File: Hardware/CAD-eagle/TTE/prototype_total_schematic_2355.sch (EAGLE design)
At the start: 46 parts, among them IC5 FT230XS, U1 LTC1069-7CS8#PBF, U3 LTC1563-2CGNSSOP-16_GN-M, U7 NX3L2467PW

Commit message: Nightly build. Hopefully final version.
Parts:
- removed C11: 100nF, SparkFun-Capacitors:22UF-0805-6.3V-20%
- removed C4, C8: 22uF, SparkFun-Capacitors:22UF-0805-6.3V-20%
- removed C9: 10nF, SparkFun-Capacitors:22UF-0805-6.3V-20%
- removed CR1: USBLC6-2SC6, TTE:USBLC6-2SC6
- removed D1, D2: (no value), diode:ZENER-DIODESMB
- removed IC5: FT230XS, ftdi:FT230XS
- removed L1: (no value), dp_devices:FERRITE-0805
- removed LED1, LED2: (no value), microbuilder:LED0805
- removed LED4: RGB, microbuilder:LED0805
- removed R10, R11: 27, microbuilder:RESISTOR0805_NOTHERMALS
- removed R12, R13, R14, R15: 10k, SparkFun-Resistors:2.0KOHM-0603-1/10W-5%
- removed R16, R7, R8, R9: 442, SparkFun-Resistors:2.0KOHM-0603-1/10W-5%
- removed R2, R6: 330, SparkFun-Resistors:2.0KOHM-0603-1/10W-5%
- removed TERMINAL_BLOCK1: ED555/2DS, DC_LOAD_AU:ED555/2DS
- removed X2: (no value), BeagleBone_Black_Wireless:GHI-CONNECTORS_10118192-0001LF
- added C17: 1.1nF, SparkFun-Capacitors:22UF-0805-6.3V-20%
- added C18: 10µF, SparkFun-Capacitors:10UF-POLAR-EIA6032-25V-10%
- added CN1: HOST, adafruit:USBMINIB
- added JP2: (no value), adafruit:PINHD-1X8-3.5MM
- added LED3, RXLED, TXLED: (no value), led:LEDCHIP-LED0603
- added R17: 1k, SparkFun-Resistors:2.0KOHM-0603-1/10W-5%
- added R18: 33k, SparkFun-Resistors:2.0KOHM-0603-1/10W-5%
- added R19: 330, SparkFun-Resistors:2.0KOHM-0603-1/10W-5%
- added R20, R25: 330, rcl:R-US_R0603
- added RIGHT_ANGLE_SMA_MALE: 5-1814400-1, TTE:5-1814400-1
- added S2: MOMENTARY-SWITCH-SPST-PTH-6.0MM, SparkFun-Switches:MOMENTARY-SWITCH-SPST-PTH-6.0MM
- added TM1: (no value), adafruit:TRIMPOTTC33X
- added U$1: AZ23C3V3, TTE:AZ23C3V3
- added U2: FT232RL-BASICSSOP, SparkFun:FT232RL-BASICSSOP
- C15: value 110n -> 470n
- C16: value 110n -> 100n
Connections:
- removed net !RESET: IC5.!RESET
- removed net 0: C11.2, C4.2, C8.2, C9.2
- removed net CTS_BAR: IC5.!CTS, R12.2
- removed net D+: C8.1, CR1.I/O2_2, R11.1, X2.SGND3
- removed net D-: C4.1, CR1.I/O1_2, R10.1, X2.SGND4
- removed net ID: X2.SGND2
- removed net N$3: LED1.A, LED2.A, R6.1
- removed net N$4: LED4.A, R2.1
- removed net N$50: U$5.P2.5/COMP1.0
- removed net PWR_EN_BAR: IC5.CBUS0
- removed net RESET_BAR: C11.1, IC5.VCCIO, R12.1, R13.1, R14.1, R15.1
- removed net RTS_BAR: IC5.!RTS, R13.2, U$5.TEST/SBWTCK
- removed net RX_LED: IC5.CBUS1, LED1.C
- removed net STATUS: IC5.CBUS2, LED2.C, LED4.C
- removed net USB_D+: IC5.USBDP, R11.2
- removed net USB_D-: IC5.USBDM, R10.2
- removed net V_BUS: C9.1, CR1.VBUS, L1.1, X2.SGND5
- new net !RTS: U$5.TEST/SBWTCK
- new net AGND_PLANE: C15.1, C16.1, U1.NC, U1.NC_2, U1.V-
- new net N$11: U7.4Z
- new net N$15: U7.3Z
- new net N$16: R19.2, S2.2
- new net N$19: LED3.A, R20.1
- new net N$20: RXLED.C, U2.RXLED
- new net N$21: TXLED.C, U2.TXLED
- new net N$22: R25.1, RXLED.A, TXLED.A
- new net N$5: U7.2S
- new net RESET: C17.1, R18.1, R19.1, U$5.RST/NMI/SBWTDIO
- new net RTS: U2.RTS
- new net STATUS_LED: R20.2, U$5.P2.5/COMP1.0
- new net USB_DATA_+: CN1.D+, U2.USBDP
- new net USB_DATA_-: CN1.D-, U2.USBDM
- new net VCC_3V3: U2.3V3OUT, U2.VCCIO
- net ANT+: now also RIGHT_ANGLE_SMA_MALE.1, U$1.1_CATHODE; no longer D2.C, TERMINAL_BLOCK1.2
- net ANT-: now also TM1.E, U$1.2_CATHODE; no longer D1.C, R16.2, R7.2, R8.2, R9.2, TERMINAL_BLOCK1.1
- net DTR: now also U2.DTR; no longer IC5.CBUS3, U$5.RST/NMI/SBWTDIO
- net FILTER_CLK: now also R17.1, R17.2
- net FILTER_IN: now also JP2.4
- net FILTER_OUT: now also JP2.5
- net FILTER_PGA_TX_OUT: now also JP2.7
- net GND: now also C17.2, C18.-, C3.1, CN1.GND, JP2.8, LED3.C, S2.1, TM1.A, U$1.COMMON_ANODE, U2.AGND, U2.GND1, U2.GND2, U2.GND3, U2.TEST; no longer C15.1, C16.1, CR1.GND, D1.A, D2.A, IC5.GND, IC5.GND@1, R16.1, R7.1, R8.1, R9.1, U1.NC, U1.NC_2, U1.V-, X2.SGND1, X2.SGND6
- net UART_BSL_RX: now also U2.TXD; no longer IC5.TXD, R15.2
- net UART_BSL_TX: now also U2.RXD; no longer IC5.RXD, R14.2
- net VCC: now also C18.+, R18.2, R25.2; no longer R2.2, R6.2
- net V_USB: now also CN1.VBUS, U2.VCC; no longer IC5.3V3OUT, IC5.VCC, L1.2
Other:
- note added: "- Using a Coaxial connection provides sheilding - 10cm has <.9dB insertion loss (1/1.11 Linear) - 30cm has <2dB insertion loss (1/1.25 Linear) https://www.thorlabs.com/newgrouppage9.cfm?objectgroup_ID=2888"
- note added: "2.2nF is upper limit, some devices use 1.1nF"
- note added: "50% duty cycle (±10%) input: 100μVRMS"
- note added: "Couple headers for good measure"
- note added: "Current Limiting Resistors, since as f-> 0, Z_L -> 0"
- note added: "Debugging"
- note added: "Design Reference: https://www.ftdichip.com/Support/Documents/DataSheets/ICs/DS_FT230X.pdf GoodFET, various models"
- note added: "Design reference: Datasheet "figure 2", pg. 6, no modifications. https://www.analog.com/media/en/technical-documentation/data-sheets/10696fa.pdf "The analog ground of the filter should be connected to the clock’s ground at a single point only""
- note added: "ID left open for USB OTG slave"
- note added: "Using a male USB port - Allows use in all weather conditions (doesn't have to be on ground) - Eliminates need for like 8 components although this guys designs are quite popular and they are never used."
- note added: "Vin must be ~.5V RMS to minimize THD + noise"
- note added: "can source 8mA or sink 1mA, so requires buffer Big THD for loads <20kohms without buffer Max 1.3mA for 80*C"
- note removed: "Current Limiting Resistors, solder in as appropriate since as f-> 0, Z_L -> 0 1 -> 7.5mA SC 2 in -> 15mA SC 4 in -> 30mA SC"
- note removed: "Design Reference: https://www.ftdichip.com/Support/Documents/DataSheets/ICs/DS_FT230X.pdf"
- note removed: "ID Left floating for slave OTG as per https://en.wikipedia.org/wiki/USB_On-The-Go"
- note removed: "Some 3V3 Zeners"

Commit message: MSP430 Initial Code, Serial Port Echo Code
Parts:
- removed C2: 100n, SparkFun-Capacitors:22UF-0805-6.3V-20%
- removed C3: 100nF, SparkFun-Capacitors:22UF-0805-6.3V-20%
- removed CN1: HOST, adafruit:USBMINIB
- removed R1, R21, R22, R3, R4, R5: Filter_R, SparkFun-Resistors:2.0KOHM-0603-1/10W-5%
- removed R19: 330, SparkFun-Resistors:2.0KOHM-0603-1/10W-5%
- removed R23, R24: 0, SparkFun-Resistors:2.0KOHM-0603-1/10W-5%
- removed TM1: (no value), adafruit:TRIMPOTTC33X
- removed U3: LTC1563-2CGNSSOP-16_GN-M, TTE:LTC1563-2CGNSSOP-16_GN-M
- added J1: (no value), SparkFun-Connectors:CONN_05X20.05_IN_PTH_SILK
- added J2: MOLEX_48037-0001MOLEX_48037-0001_0_0, TTE:MOLEX_48037-0001MOLEX_48037-0001_0_0
- added TM2: (no value), adafruit:TRIMPOTTC33X
- C1: value 100n -> 100nF
- C17: value 1.1nF -> 1000p
- R18: value 33k -> 47k
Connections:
- net N$51 renamed SPI_SCL
- net N$52 renamed SPI_SDA
- net N$53 renamed SPI_CLK
- net N$54 renamed SPI_CS
- net OA3- renamed N$2
- removed net !RTS: U$5.TEST/SBWTCK
- removed net AGND_PLANE: C15.1, C16.1, U1.NC, U1.NC_2, U1.V-
- removed net DTR: U2.DTR
- removed net FILTER_EN: U3.!EN
- removed net FILTER_INVB1: R4.2, U3.INVB
- removed net FILTER_LPA: R1.1, R22.2, U3.LPA
- removed net FILTER_SB1: R22.1, R4.1, R5.1, U3.SB
- removed net N$10: U$5.P4.0/UCA1STE/ISOTXD/ISORXD
- removed net N$12: C1.2, U3.AGND
- removed net N$13: U$5.P2.3/TB1TRG
- removed net N$14: U$5.P2.2/TB1CLK
- removed net N$16: R19.2, S2.2
- removed net N$17: U$5.P1.1/UCB0CLK/ACLK/OA0O/COMP0.1/A1
- removed net N$2 (its old number): U$5.P4.3/UCA1TXD/UCA1SIMO/UCA1TXD
- removed net N$23: U$5.P2.1/TB1.2/COMP1.O
- removed net N$32: U$5.P3.4/SMCLK
- removed net N$33: U$5.P5.1/TB2.2/MFM.TX/A9
- removed net N$38: U$5.P3.0/MCLK
- removed net N$47: U$5.P2.6/MCLK/XOUT
- removed net N$48: U$5.P2.7/TB0CLK/XIN
- removed net N$49: U$5.P2.4/COMP1.1
- removed net N$6: U$5.P4.1/UCA1CLK
- removed net N$7: R1.2, R21.1, R3.2, U3.SA
- removed net N$8: U$5.P4.2/UCA1RXD/UCA1SOMI/UCA1RXD
- removed net N$9: R3.1, U3.INVA
- removed net RESET: C17.1, R18.1, R19.1, U$5.RST/NMI/SBWTDIO
- removed net RTS: U2.RTS
- removed net RX_INPUT_+: U$5.P1.3/UCB0SOMI/UCB0SCL/OA0+/A3, U$5.P1.5/UCA0CLK/TMS/OA1O/A5, U$5.P3.3/OA2+, U7.1Y1
- removed net RX_INPUT_-_DECOUPLED: C3.2, U$5.P3.2/OA2-
- removed net UART_BSL_RX: U$5.P1.6/UCA0RXD/UCA0SOMI/TB0.1/TDI/TCLK/OA1-/A6, U2.TXD
- removed net UART_BSL_TX: U$5.P1.7/UCA0TXD/UCA0SIMO/TB0.2/TDO/OA1+/A7/VREF+, U2.RXD
- new net !RTS!_JTAG_TCK: J1.7, U$5.TEST/SBWTCK, U2.RTS
- new net JTAG_TCK: J1.4, U$5.P1.4/UCA0STE/TCK/A4
- new net N$3: C15.2, U1.AGND
- new net RESET_JTAG_RESET: C17.1, J1.10, R18.1, S2.2, U$5.RST/NMI/SBWTDIO, U2.DTR
- new net RX_INPUT_DAC_JTAG_TMS: C1.2, J1.2, JP2.6, U$5.P1.5/UCA0CLK/TMS/OA1O/A5, U$5.P3.3/OA2+
- new net UART_BSL_RX_JTAG_DIN: J1.8, JP2.2, U$5.P1.6/UCA0RXD/UCA0SOMI/TB0.1/TDI/TCLK/OA1-/A6, U$5.P4.2/UCA1RXD/UCA1SOMI/UCA1RXD, U2.TXD
- new net UART_BSL_TX_JTAG_DOUT: J1.6, JP2.3, U$5.P1.7/UCA0TXD/UCA0SIMO/TB0.2/TDO/OA1+/A7/VREF+, U$5.P4.3/UCA1TXD/UCA1SIMO/UCA1TXD, U2.RXD
- net AGND: now also C15.1, C16.1, U1.NC, U1.NC_2, U1.V-; no longer C15.2, U1.AGND
- net ANT-: no longer TM1.E, U7.2Y1
- net FILTER_IN: no longer R21.2
- net FILTER_OUT: no longer R5.2, U3.LPB
- net FILTER_PGA_TX_OUT: now also TM2.A, TM2.S
- net GND: now also J1.3, J1.5, J1.9, J2.4, J2.MNT_1, J2.MNT_2, U$5.P3.2/OA2-; no longer C1.1, C2.1, C3.1, CN1.GND, R23.2, R24.1, R24.2, TM1.A, U3.!LP, U3.NC, U3.NC_2, U3.NC_3, U3.NC_4, U3.NC_5, U3.V-, U7.2Y0
- net N$1: now also C1.1, U7.1Y1; no longer U$5.P1.2/UCB0SIMO/UCB0SDA/TB0TRG/OA0-/A2/VEREF
- net TX_RX_ANTENNA_SELECT: now also U$5.P5.1/TB2.2/MFM.TX/A9
- net USB_DATA_+: now also J2.2; no longer CN1.D+
- net USB_DATA_-: now also J2.3; no longer CN1.D-
- net VCC: now also J1.1; no longer C2.2, R23.1, U3.V+
- net V_USB: now also J2.1, JP2.1; no longer CN1.VBUS
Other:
- note added: "JTAG Interface (incase other programming doesn't work :C)"
- note removed: "2.2nF is upper limit, some devices use 1.1nF"
- note removed: "DAC"
- note removed: "ID left open for USB OTG slave"
- note removed: "Low Power Mode has better THD & less power consumption by an order of magnitude Nonetheless, jumper left here to allow mode to be changed dynamically"
- note removed: "https://www.electronics-notes.com/articles/electronic_components/resistors/standard-resistor-values-e-series-e3-e6-e12-e24-e48-e96.php Choose resistor value from here 15kOhm -> fc = 17.06kHz, f50dB"

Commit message: Submitted orderss. finally. :)
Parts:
- removed C13: 100nF, SparkFun-Capacitors:22UF-0805-6.3V-20%
- removed C14: 22uF, SparkFun-Capacitors:22UF-0805-6.3V-20%
- removed C15: 470n, SparkFun-Capacitors:22UF-0805-6.3V-20%
- removed C16: 100n, SparkFun-Capacitors:22UF-0805-6.3V-20%
- removed C17: 1000p, SparkFun-Capacitors:22UF-0805-6.3V-20%
- removed C18: 10µF, SparkFun-Capacitors:10UF-POLAR-EIA6032-25V-10%
- removed J1: (no value), SparkFun-Connectors:CONN_05X20.05_IN_PTH_SILK
- removed JP2: (no value), adafruit:PINHD-1X8-3.5MM
- removed LED3, RXLED, TXLED: (no value), led:LEDCHIP-LED0603
- removed R17: 1k, SparkFun-Resistors:2.0KOHM-0603-1/10W-5%
- removed R18: 47k, SparkFun-Resistors:2.0KOHM-0603-1/10W-5%
- removed R20, R25: 330, rcl:R-US_R0603
- removed S2: MOMENTARY-SWITCH-SPST-PTH-6.0MM, SparkFun-Switches:MOMENTARY-SWITCH-SPST-PTH-6.0MM
- removed U$1: AZ23C3V3, TTE:AZ23C3V3
- removed U$5: MSP430FR2355, TTE:MSP430FR2355
- removed U1: LTC1069-7CS8#PBF, TTE:LTC1069-7CS8#PBF
- removed U2: FT232RL-BASICSSOP, SparkFun:FT232RL-BASICSSOP
- removed U7: NX3L2467PW, TTE:NX3L2467PW
- added 1K: 1k, microbuilder:RESISTOR0805
- added 47K: 47k, microbuilder:RESISTOR0805
- added C2: 100nF, SparkFun-Capacitors:22UF-0805-6.3V-20%
- added C3: 22uF, SparkFun-Capacitors:22UF-0805-6.3V-20%
- added C4: 470n, SparkFun-Capacitors:22UF-0805-6.3V-20%
- added C5: 100n, SparkFun-Capacitors:22UF-0805-6.3V-20%
- added D1: 3.3V, SparkFun-DiscreteSemi:DIODE-ZENER-MM3Z3V3T1G
- added FILT: FILT, SparkFun-Connectors:CONN_02
- added FT232RL: FT232RL-BASICSSOP, SparkFun:FT232RL-BASICSSOP
- added GND, RXD, TCK, TDIO, TXD, VCC: 455-1750-1-ND, SparkFun-Connectors:CONN_04
- added J4, SIG: RX, SparkFun-Connectors:CONN_02
- added MSP430: MSP430FR2355, TTE:MSP430FR2355
- added R2, R6: 330, microbuilder:RESISTOR0805
- added R4: 1M, SparkFun-Resistors:2.0KOHM-0603-1/10W-5%
- added RST: MOMENTARY-SWITCH-SPST-PTH-6.0MM, SparkFun-Switches:MOMENTARY-SWITCH-SPST-PTH-6.0MM
- added RX, STATUS, TX: (no value), microbuilder:LED0805
- added TL069: LTC1069-7CS8#PBF, TTE:LTC1069-7CS8#PBF
- C1: value 100nF -> 10µF; device SparkFun-Capacitors:22UF-0805-6.3V-20% -> SparkFun-Capacitors:10UF-POLAR-EIA6032-25V-10%
- C6: value 100nF -> 1n
- TM2: value (none) -> 100
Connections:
- removed net !RTS!_JTAG_TCK: J1.7, U$5.TEST/SBWTCK, U2.RTS
- removed net AGND: C15.1, C16.1, U1.NC, U1.NC_2, U1.V-
- removed net ANT+: RIGHT_ANGLE_SMA_MALE.1, U$1.1_CATHODE, U7.2Z
- removed net ANT-: U$1.2_CATHODE
- removed net FILTER_PGA_TX_OUT: JP2.7, TM2.A, TM2.S, U$5.P3.5/OA3O, U$5.P5.0/TB2.1/MFM.RX/A8, U7.1Y0
- removed net JTAG_TCK: J1.4, U$5.P1.4/UCA0STE/TCK/A4
- removed net N$11: U7.4Z
- removed net N$15: U7.3Z
- removed net N$2: U$5.P3.6/OA3-
- removed net N$5: U7.2S
- removed net OA2+: U7.1Z
- removed net RESET_JTAG_RESET: C17.1, J1.10, R18.1, S2.2, U$5.RST/NMI/SBWTDIO, U2.DTR
- removed net RX_INPUT_DAC_JTAG_TMS: C1.2, J1.2, JP2.6, U$5.P1.5/UCA0CLK/TMS/OA1O/A5, U$5.P3.3/OA2+
- removed net SPI_CLK: U$5.P4.5/UCB1CLK
- removed net SPI_CS: U$5.P4.4/UCB1STE
- removed net SPI_SCL: U$5.P4.7/UCB1SOMI/UCB1SCL
- removed net SPI_SDA: U$5.P4.6/UCB1SIMO/UCB1SDA
- removed net TX_RX_ANTENNA_SELECT: U$5.P5.1/TB2.2/MFM.TX/A9, U7.1S
- removed net UART_BSL_RX_JTAG_DIN: J1.8, JP2.2, U$5.P1.6/UCA0RXD/UCA0SOMI/TB0.1/TDI/TCLK/OA1-/A6, U$5.P4.2/UCA1RXD/UCA1SOMI/UCA1RXD, U2.TXD
- removed net UART_BSL_TX_JTAG_DOUT: J1.6, JP2.3, U$5.P1.7/UCA0TXD/UCA0SIMO/TB0.2/TDO/OA1+/A7/VREF+, U$5.P4.3/UCA1TXD/UCA1SIMO/UCA1TXD, U2.RXD
- removed net VCC_3V3: U2.3V3OUT, U2.VCCIO
- removed net V_CM: U$5.P1.0/UCB0STE/SMCLK/COMP0.0/A0/VEREF+
- new net ADC: J4.2, MSP430.P1.1/UCB0CLK/ACLK/OA0O/COMP0.1/A1, MSP430.P1.2/UCB0SIMO/UCB0SDA/TB0TRG/OA0-/A2/VEREF
- new net ANTENNA_SIG: D1.C, MSP430.P3.3/OA2+, R4.1, RIGHT_ANGLE_SMA_MALE.1, SIG.1, TM2.A
- new net ANTENNA_TX_SIG: MSP430.P3.5/OA3O, SIG.2, TM2.E
- new net BCLUART_RXD: MSP430.P1.6/UCA0RXD/UCA0SOMI/TB0.1/TDI/TCLK/OA1-/A6, MSP430.P4.2/UCA1RXD/UCA1SOMI/UCA1RXD, RXD.2
- new net BCLUART_RXD_EXT: RXD.3, RXD.4
- new net BCLUART_RXD_USB: FT232RL.TXD, RXD.1
- new net BCLUART_TXD: MSP430.P1.7/UCA0TXD/UCA0SIMO/TB0.2/TDO/OA1+/A7/VREF+, MSP430.P4.3/UCA1TXD/UCA1SIMO/UCA1TXD, TXD.2
- new net BCLUART_TXD_EXT: TXD.3, TXD.4
- new net BCLUART_TXD_USB: FT232RL.RXD, TXD.1
- new net GND_EXT: GND.3, GND.4
- new net GND_USB: GND.1
- new net RST/SBWTDIO: 47K.1, C6.1, MSP430.RST/NMI/SBWTDIO, RST.2, TDIO.2
- new net RST/SBWTDIO_EXT: TDIO.3, TDIO.4
- new net RST/SBWTDIO_USB: FT232RL.DTR, TDIO.1
- new net RX_PGA_1: J4.1, MSP430.P1.3/UCB0SOMI/UCB0SCL/OA0+/A3, MSP430.P3.1/OA2O
- new net TEST/SSBWTCK: MSP430.TEST/SBWTCK, TCK.2
- new net TEST/SSBWTCK_USB: FT232RL.RTS, TCK.1
- new net TST/SBWTCK_EXT: TCK.3, TCK.4
- new net VCC_EXT: VCC.3, VCC.4
- new net VCC_USB: FT232RL.3V3OUT, FT232RL.VCCIO, VCC.1
- net FILTER_CLK: now also 1K.1, MSP430.P2.1/TB1.2/COMP1.O; no longer R17.1, R17.2, U$5.P2.0/TB1.1/COMP0.O, U1.CLK
- net FILTER_IN: now also FILT.2, MSP430.P1.5/UCA0CLK/TMS/OA1O/A5, MSP430.P5.0/TB2.1/MFM.RX/A8, TL069.VIN; no longer JP2.4, U$5.P3.1/OA2O, U1.VIN
- net FILTER_OUT: now also FILT.1, MSP430.P3.7/OA3+, TL069.VOUT; no longer JP2.5, U$5.P3.7/OA3+, U1.VOUT
- net GND: now also C1.-, C2.2, C3.2, C4.1, C5.1, D1.A, FT232RL.AGND, FT232RL.GND1, FT232RL.GND2, FT232RL.GND3, FT232RL.TEST, GND.2, MSP430.DVSS, R4.2, RIGHT_ANGLE_SMA_MALE.2, RST.1, STATUS.C, TL069.NC, TL069.NC_2, TL069.V-; no longer C13.2, C14.2, C17.2, C18.-, J1.3, J1.5, J1.9, JP2.8, LED3.C, S2.1, U$1.COMMON_ANODE, U$5.DVSS, U$5.P3.2/OA2-, U2.AGND, U2.GND1, U2.GND2, U2.GND3, U2.TEST, U7.GND
- net N$1: now also 1K.2, TL069.CLK; no longer C1.1, U7.1Y1
- net N$19: now also R2.1, STATUS.A; no longer LED3.A, R20.1
- net N$20: now also FT232RL.RXLED, RX.C; no longer RXLED.C, U2.RXLED
- net N$21: now also FT232RL.TXLED, TX.C; no longer TXLED.C, U2.TXLED
- net N$22: now also R6.1, RX.A, TX.A; no longer R25.1, RXLED.A, TXLED.A
- net N$3: now also C4.2, TL069.AGND; no longer C15.2, U1.AGND
- net STATUS_LED: now also MSP430.P2.5/COMP1.0, R2.2; no longer R20.2, U$5.P2.5/COMP1.0
- net USB_DATA_+: now also FT232RL.USBDP; no longer U2.USBDP
- net USB_DATA_-: now also FT232RL.USBDM; no longer U2.USBDM
- net VCC: now also 47K.2, C1.+, C2.1, C3.1, C5.2, MSP430.DVCC, R6.2, TL069.V+, VCC.2; no longer C13.1, C14.1, C16.2, C18.+, C6.1, J1.1, R18.2, R25.2, U$5.DVCC, U1.V+, U7.VCC
- net V_USB: now also FT232RL.VCC; no longer JP2.1, U2.VCC
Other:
- note removed: "ADC"
- note removed: "JTAG Interface (incase other programming doesn't work :C)"
- note removed: "Looks a little weird but trace through the signal names"
- moved on the sheet: C6, J2, TM2

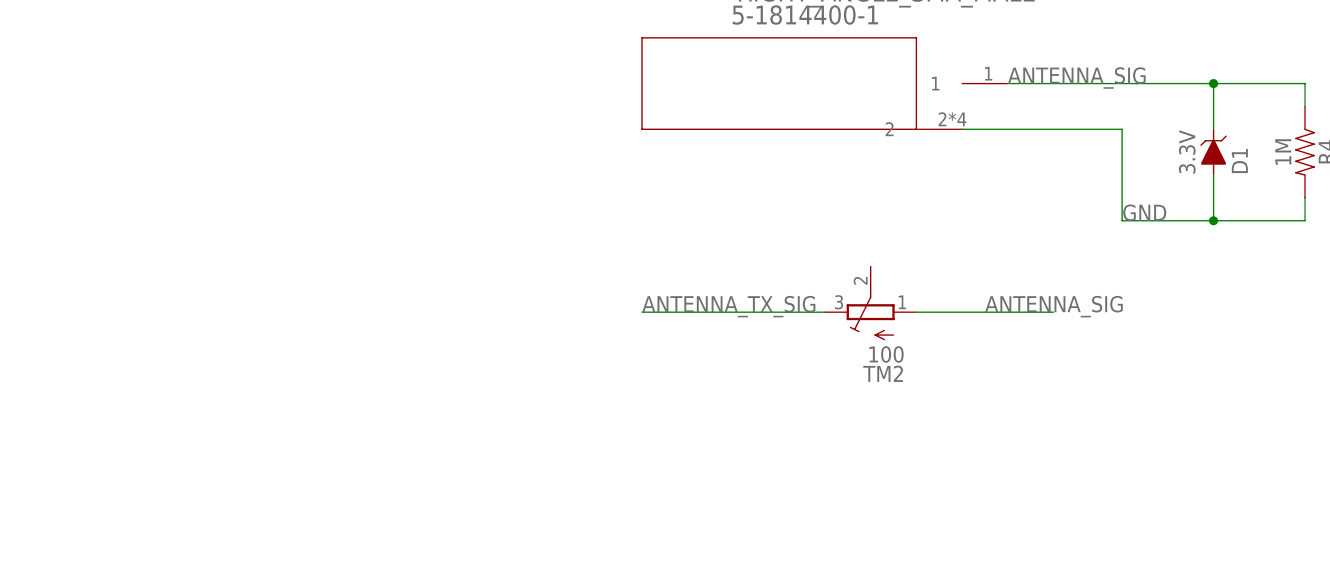
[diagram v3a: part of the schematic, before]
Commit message: Cascaded RX PGA array confirmed
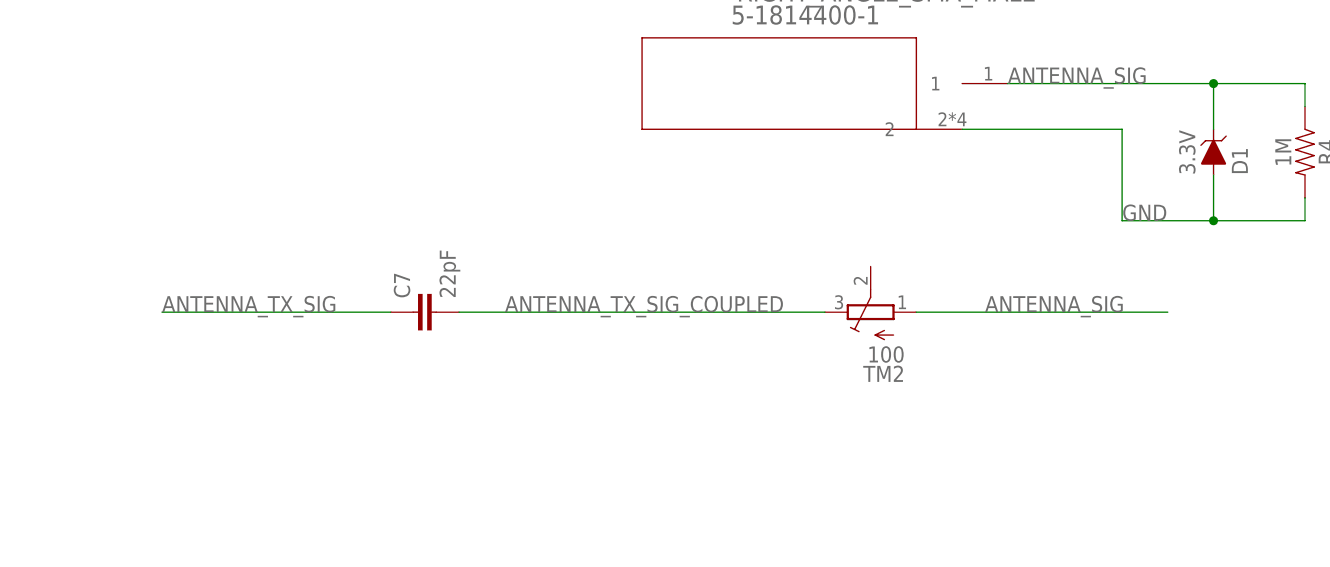
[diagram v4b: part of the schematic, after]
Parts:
- added C7: 22pF, SparkFun-Capacitors:22UF-0805-6.3V-20%
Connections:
- new net ANTENNA_TX_SIG_COUPLED: C7.2, TM2.E
- net ANTENNA_TX_SIG: now also C7.1; no longer TM2.E
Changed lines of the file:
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@@
 <part name="VCC" library="SparkFun-Connectors" deviceset="CONN_04" device="" value="455-1750-1-ND"/>
 <part name="GND" library="SparkFun-Connectors" deviceset="CONN_04" device="" value="455-1750-1-ND"/>
+<part name="C7" library="SparkFun-Capacitors" deviceset="22UF" device="-0805-6.3V-20%" value="22pF"/>
 </parts>
 <sheets>
@@
 <instance part="VCC" gate="G$1" x="185.42" y="-111.76"/>
 <instance part="GND" gate="G$1" x="185.42" y="-129.54"/>
+<instance part="C7" gate="G$1" x="-208.28" y="35.56" rot="R90"/>
 </instances>
 <busses>
@@
 <segment>
 <pinref part="TM2" gate="G$1" pin="A"/>
-<wire x1="-154.94" y1="35.56" x2="-139.7" y2="35.56" width="0.1524" layer="91"/>
+<wire x1="-154.94" y1="35.56" x2="-127" y2="35.56" width="0.1524" layer="91"/>
 <label x="-147.32" y="35.56" size="1.778" layer="95"/>
 </segment>
@@
 </segment>
 <segment>
-<label x="-185.42" y="35.56" size="1.778" layer="95"/>
-<pinref part="TM2" gate="G$1" pin="E"/>
-<wire x1="-185.42" y1="35.56" x2="-165.1" y2="35.56" width="0.1524" layer="91"/>
-</segment>
-<segment>
 <label x="177.8" y="-10.16" size="1.778" layer="95"/>
 <wire x1="177.8" y1="-10.16" x2="218.44" y2="-10.16" width="0.1524" layer="91"/>
 <pinref part="SIG" gate="G$1" pin="2"/>
+</segment>
+<segment>
+<pinref part="C7" gate="G$1" pin="1"/>
+<wire x1="-213.36" y1="35.56" x2="-238.76" y2="35.56" width="0.1524" layer="91"/>
+<label x="-238.76" y="35.56" size="1.778" layer="95"/>
 </segment>
 </net>
@@
 </segment>
 </net>
+<net name="ANTENNA_TX_SIG_COUPLED" class="0">
+<segment>
+<label x="-200.66" y="35.56" size="1.778" layer="95"/>
+<pinref part="TM2" gate="G$1" pin="E"/>
+<pinref part="C7" gate="G$1" pin="2"/>
+<wire x1="-205.74" y1="35.56" x2="-165.1" y2="35.56" width="0.1524" layer="91"/>
+</segment>
+</net>
